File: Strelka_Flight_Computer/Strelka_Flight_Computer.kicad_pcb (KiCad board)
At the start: 4 copper layers, 91 x 30.1 mm, 165 parts, among them IC1 XTSD04GLGEAG, IC2 MAX-M10S-00B, J2 Conn_01x04, J3 DB125-3.5-4P-GN-S, J4 SM06B-GHS-TB(LF)(SN), J6 USB_B_Micro, J7 Conn_01x02, J8 Conn_01x07, Q1 CJK2333, Q10 AP2300, Q11 MMBT2222, Q15 AO3400A, Q16 AO3400A, Q17 AO3401A, Q2 CJK2333, Q4 AO3401A, Q5 AP2300, Q6 MMBT2222, Q9 AO3401A, SW1 SW_DIP_x01, SW6 TS-1185-C-A-A-A, SW7 TS-1185-C-A-A-A, U1 ASM330LHHXTR, U11 BMX055, U12 MS561101BA03-50, U16 TPS61085DGKR, U2 AP9101CK6, U3 AMS1117-3.3, U4 RFM95W-915S2, U5 MCP2551-I-SN, U6 STM32H743VITx, U8 USBLC6-2SC6, Y5 Q13FC1350000400, Y6 X1E0000210834

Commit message: Via stitched
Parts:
- removed TP11, TP2, TP5, TP6, TP7, TP8: TestPoint, TestPoint:TestPoint_Pad_1.0x1.0mm
- C10, C2, C28, C29, C30, C31, C39, C4: value 100nF -> 100n
- C11, C3, C40, C7, C8: value 10uF -> 10u
- moved TP9 98.4 mm to (169.3, 70.5)
- moved TP10 95.3 mm to (171.5, 70.5)
- moved TP4 52.3 mm to (103.0, 67.0)
- moved TP3 49.1 mm to (101.0, 67.0)
- moved TP1 45.9 mm to (99.0, 67.0)
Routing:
- net +5VA: track 25.4 -> 48.8 mm, vias 3 -> 4
- net /STM32H743/USART2_TX: track 29.0 -> 47.8 mm, vias 0 -> 2
- net /STM32H743/USART2_RX: track 26.0 -> 41.2 mm, vias 0 -> 2
- net VDC: track 59.5 -> 71.9 mm
- net +3.3V: track 77.1 -> 85.5 mm
- net GND: track 54.3 -> 55.4 mm, vias 70 -> 98
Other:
- board text added: "+3.3V"
- board text added: "+5VA"
- board text added: "Rx"
- board text added: "Tx"
- board text added: "VDC"

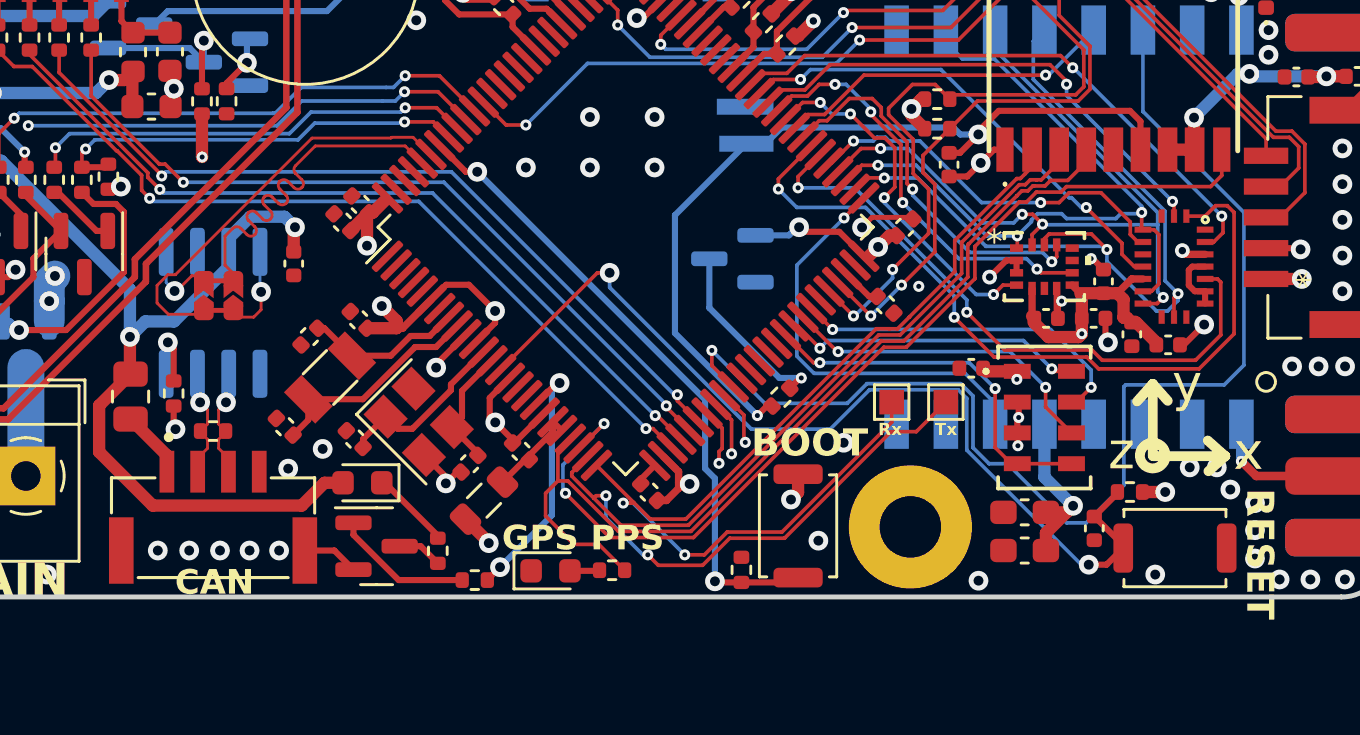
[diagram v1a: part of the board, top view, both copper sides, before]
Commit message: Added lp filter caps to adc signals
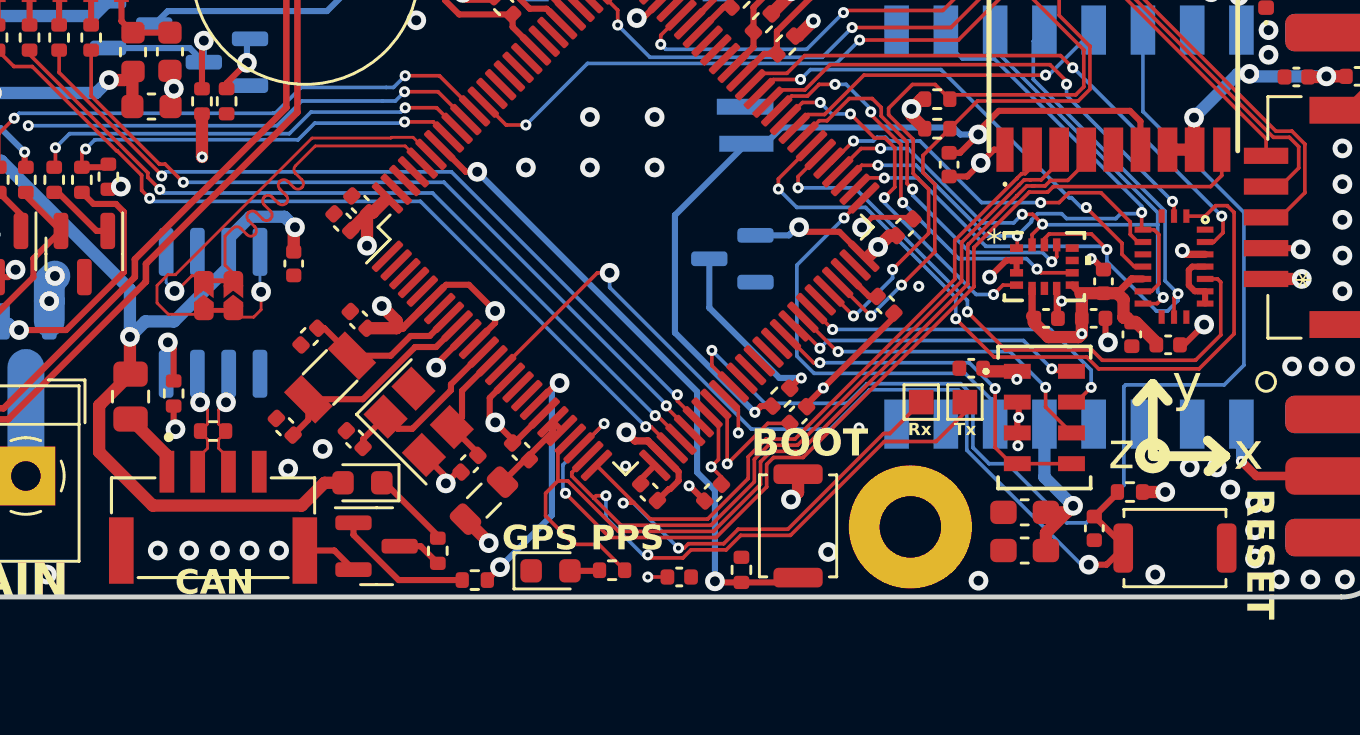
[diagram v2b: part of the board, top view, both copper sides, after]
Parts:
- added C12: 10n, Capacitor_SMD:C_0402_1005Metric, F.Cu at (165.5, 71.0)
- added C13: 10n, Capacitor_SMD:C_0402_1005Metric, F.Cu at (160.7, 77.6)
- added C9: 10n, Capacitor_SMD:C_0402_1005Metric, F.Cu at (162.1, 74.2)
- moved TP9 1.20 mm to (170.5, 70.5)
- moved TP10 0.78 mm to (172.3, 70.5)
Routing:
- net GND: track 55.4 -> 61.6 mm, vias 98 -> 101
- net /Actuators/MAIN_CONT: track 57.7 -> 61.8 mm, vias 2 -> 3
- net /Actuators/DROGUE_CONT: track 58.3 -> 61.1 mm
- net /STM32H743/USART2_TX: track 47.8 -> 49.3 mm
- net +3.3V: track 85.5 -> 86.7 mm
- net /STM32H743/USART2_RX: track 41.2 -> 42.4 mm
- net /Sensors/MAX-M10S-00B/PPS: track 37.4 -> 38.1 mm
- net /STM32H743/GPS_RST: track 40.3 -> 41.0 mm
- net /Power/BATT_VOLT: track 63.9 -> 64.6 mm

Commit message: Added LCSC mpn to all relevent parts
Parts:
- removed C56: 47u, Capacitor_SMD:C_0805_2012Metric
- added C14: 22u, Capacitor_SMD:C_0805_2012Metric, F.Cu at (129.5, 68.7)
- C10: footprint Capacitor_SMD:C_0603_1608Metric_Pad1.08x0.95mm_HandSolder -> Capacitor_SMD:C_0402_1005Metric
- C55: value 47u -> 22u
- R18, R19, R21, R65: value 33 -> 33R
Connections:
- U6 pad 84: unconnected-(U6-PD3-Pad84) -> /915MHz_Radio/IO1_RF
- U6 pad 85: unconnected-(U6-PD4-Pad85) -> /915MHz_Radio/IO2_RF
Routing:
- net /915MHz_Radio/IO1_RF: track 0.00 -> 27.1 mm, vias 0 -> 2
- net /915MHz_Radio/IO2_RF: track 0.00 -> 23.9 mm, vias 0 -> 2
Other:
- board text added: "Created by Angus McLennan Oct 2023"
- board text added: "JLCJLCJLC"

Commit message: Finalised BOM and sent order:
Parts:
- removed JP4: UART_Switch, Footprints:UART_Switch
- added C15: 4.7n, Capacitor_SMD:C_0603_1608Metric, F.Cu at (142.3, 69.0)
- added D7: SP0504BAJT, Package_TO_SOT_SMD:SOT-353_SC-70-5, F.Cu at (142.3, 64.3)
- added FL1: 744231121, Footprints:CHIP_31121_WRE, F.Cu at (142.3, 67.0)
- added R26: 60R4, Resistor_SMD:R_0402_1005Metric, F.Cu at (142.8, 70.8)
- R13: value 120R -> 60R4
- moved C1 1.43 mm to (145.0, 66.3)
- moved R13 0.88 mm to (141.8, 70.8), turned to 90 degrees
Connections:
- R13 pad 2: /Data_Interfaces/CAN_- -> /Data_Interfaces/tap
- U5 pad 1: Net-(JP4-RX1) -> /Data_Interfaces/CAN_TXD
- U5 pad 4: Net-(JP4-TX1) -> /Data_Interfaces/CAN_RXD
- U5 pad 6: /Data_Interfaces/CAN_- -> /Data_Interfaces/CANL
- U5 pad 7: /Data_Interfaces/CAN_+ -> /Data_Interfaces/CANH
- U6 pad 95: /Data_Interfaces/CAN_N -> /Data_Interfaces/CAN_RXD
- U6 pad 96: /Data_Interfaces/CAN_P -> /Data_Interfaces/CAN_TXD
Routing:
- net /Data_Interfaces/CAN_N: track 16.5 -> 0.00 mm
- net /Data_Interfaces/CAN_P: track 16.4 -> 0.00 mm
- net /Data_Interfaces/CAN_TXD: track 0.00 -> 12.5 mm, vias 0 -> 1
- net /Data_Interfaces/CAN_RXD: track 0.00 -> 9.85 mm, vias 0 -> 1
- net /Data_Interfaces/CAN_-: track 4.55 -> 11.2 mm, vias 1 -> 0
- net /Data_Interfaces/CANH: track 0.00 -> 5.10 mm, vias 0 -> 1
- net /Data_Interfaces/CAN_+: track 4.55 -> 9.46 mm, vias 1 -> 0
- net +5V: track 82.5 -> 86.8 mm
- net Net-(JP4-TX1): track 3.47 -> 0.00 mm, vias 1 -> 0
- net GND: track 61.6 -> 65.1 mm, vias 101 -> 103
- net Net-(JP4-RX1): track 3.05 -> 0.00 mm, vias 1 -> 0
- net /Data_Interfaces/CANL: track 0.00 -> 2.61 mm, vias 0 -> 1
- net /Data_Interfaces/tap: track 0.00 -> 2.33 mm
- net /Actuators/EXT_SPI_CS: track 34.4 -> 35.4 mm
- net /Actuators/EXT_SPI_SCK: track 33.2 -> 34.2 mm
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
